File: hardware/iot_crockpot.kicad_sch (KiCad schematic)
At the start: 18 parts, among them J1 Screw_Terminal_01x02, K1 G5LE-1, K2 G5LE-1, Q1 2N7002, Q2 2N7002, U3 MAX31855KASA

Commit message: Schematic Updates - Power Supply
Added architecture for power supply to schematic.
Need to rethink control architecture. There is only two I/O exposed on
CYD. May use second MCU on control board flashed and controlled over
I2C by CYD.
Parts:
- added F2: Fuse, symbol Device:Fuse
- added F3: 1.5A, Fuse:Fuse_1206_3216Metric_Pad1.42x1.75mm_HandSolder, symbol Device:Polyfuse
- added J2: Screw_Terminal_01x02, symbol Connector:Screw_Terminal_01x02
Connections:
- net +5V: now also F3.2; no longer PS1.4 (+Vout)
- net NEUTRAL: now reaches C1.2, FL1.3, J1.1 (Pin_1), RV1.2
- net HOT: now reaches F1.1, J1.2 (Pin_2)
- new net: F3.1, PS1.4 (+Vout)
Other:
- note added: "120VAC INPUT"
- moved on the sheet: J1

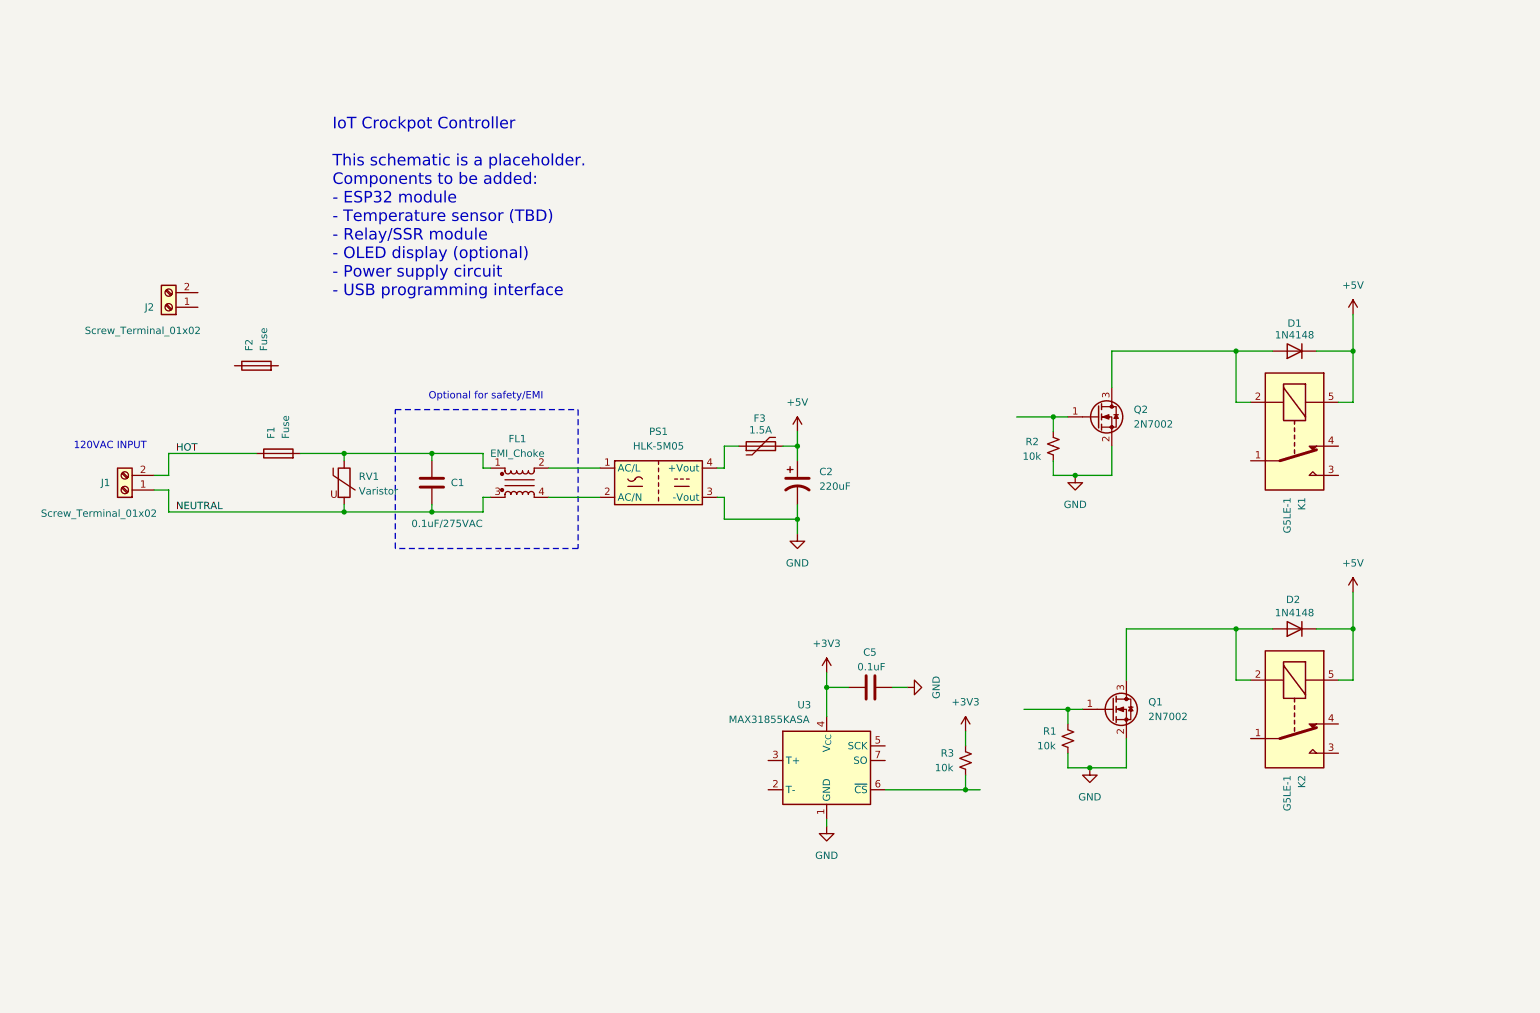
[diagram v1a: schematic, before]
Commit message: Added MCU to schematic
Added MCU to schematic and organized circuits into blocks
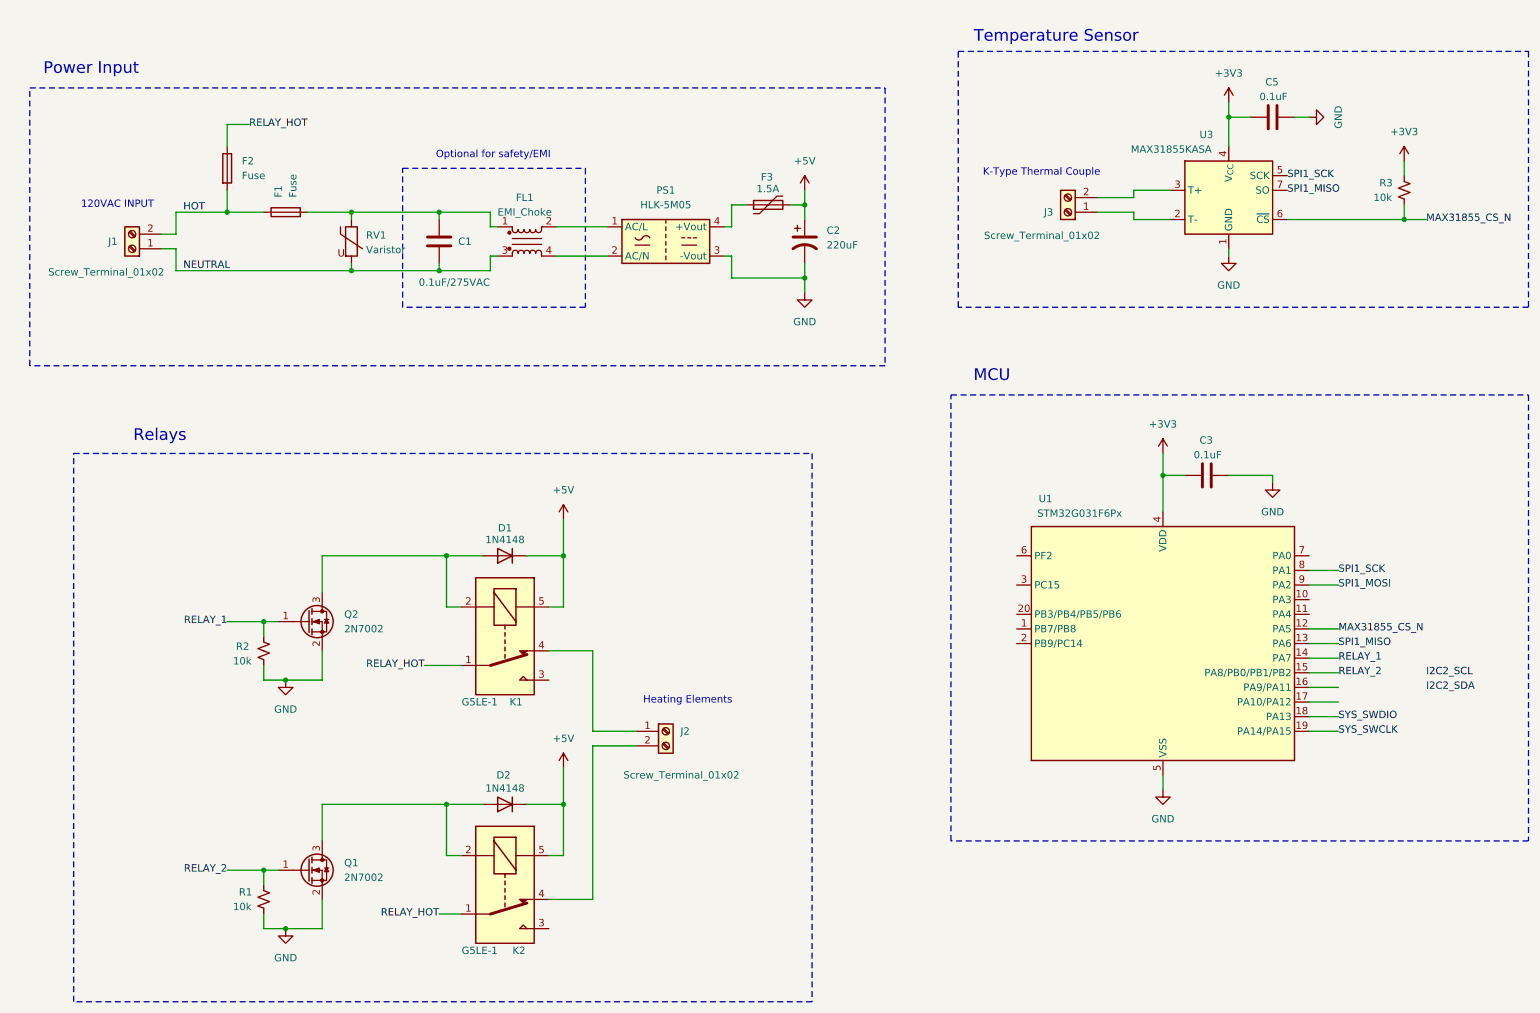
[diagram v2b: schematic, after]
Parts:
- added C3: 0.1uF, symbol Device:C
- added J3: Screw_Terminal_01x02, symbol Connector:Screw_Terminal_01x02
- added U1: STM32G031F6Px, Package_SO:TSSOP-20_4.4x6.5mm_P0.65mm, symbol MCU_ST_STM32G0:STM32G031F6Px
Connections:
- net +3V3: now also C3.1, U1.4 (VDD)
- net GND: now also C3.2, U1.5 (VSS)
- net HOT: now also F2.2
- net RELAY_1: now reaches Q2.1 (G), R2.1
- net RELAY_1: now also U1.14 (PA7)
- net RELAY_HOT: now reaches K2.1
- net RELAY_HOT: now also F2.1, K1.1
- net at K2.4: now also J2.2 (Pin_2)
- net at J2.1 (Pin_1): now also K1.4
- net at U3.2 (T-): now also J3.1 (Pin_1)
- net at U3.3 (T+): now also J3.2 (Pin_2)
- net SPI1_SCK: now reaches U3.5 (SCK)
- net SPI1_SCK: now also U1.8 (PA1)
- net MAX31855_CS_N: now reaches R3.2, U3.6 (~{CS})
- net MAX31855_CS_N: now also U1.12 (PA5)
- net SPI1_MISO: now reaches U3.7 (SO)
- net SPI1_MISO: now also U1.13 (PA6)
- net RELAY_2: now reaches Q1.1 (G), R1.1
- net RELAY_2: now also U1.15 (PA8/PB0/PB1/PB2)
- new net SPI1_MOSI: U1.9 (PA2)
- new net SYS_SWCLK: U1.19 (PA14/PA15)
- new net SYS_SWDIO: U1.18 (PA13)
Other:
- note added: "Heating Elements"
- note added: "K-Type Thermal Couple"
- note added: "MCU"
- note added: "Power Input"
- note added: "Relays"
- note added: "Temperature Sensor"
- note removed: "IoT Crockpot Controller This schematic is a placeholder. Components to be added: - ESP32 module - Temperature sensor (TBD) - Relay/SSR module - OLED display (optional) - Power supply circuit - USB programming interface"
- moved on the sheet: C1, C2, C5, D1, D2, F1, F2, F3, FL1, J1, J2, K1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

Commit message: More Passive Part Selection
Added passive parts/numbers and models to schematic.
Started rough outline of PCB. Considerations will need to be done for
angle of display in relation to height of components.
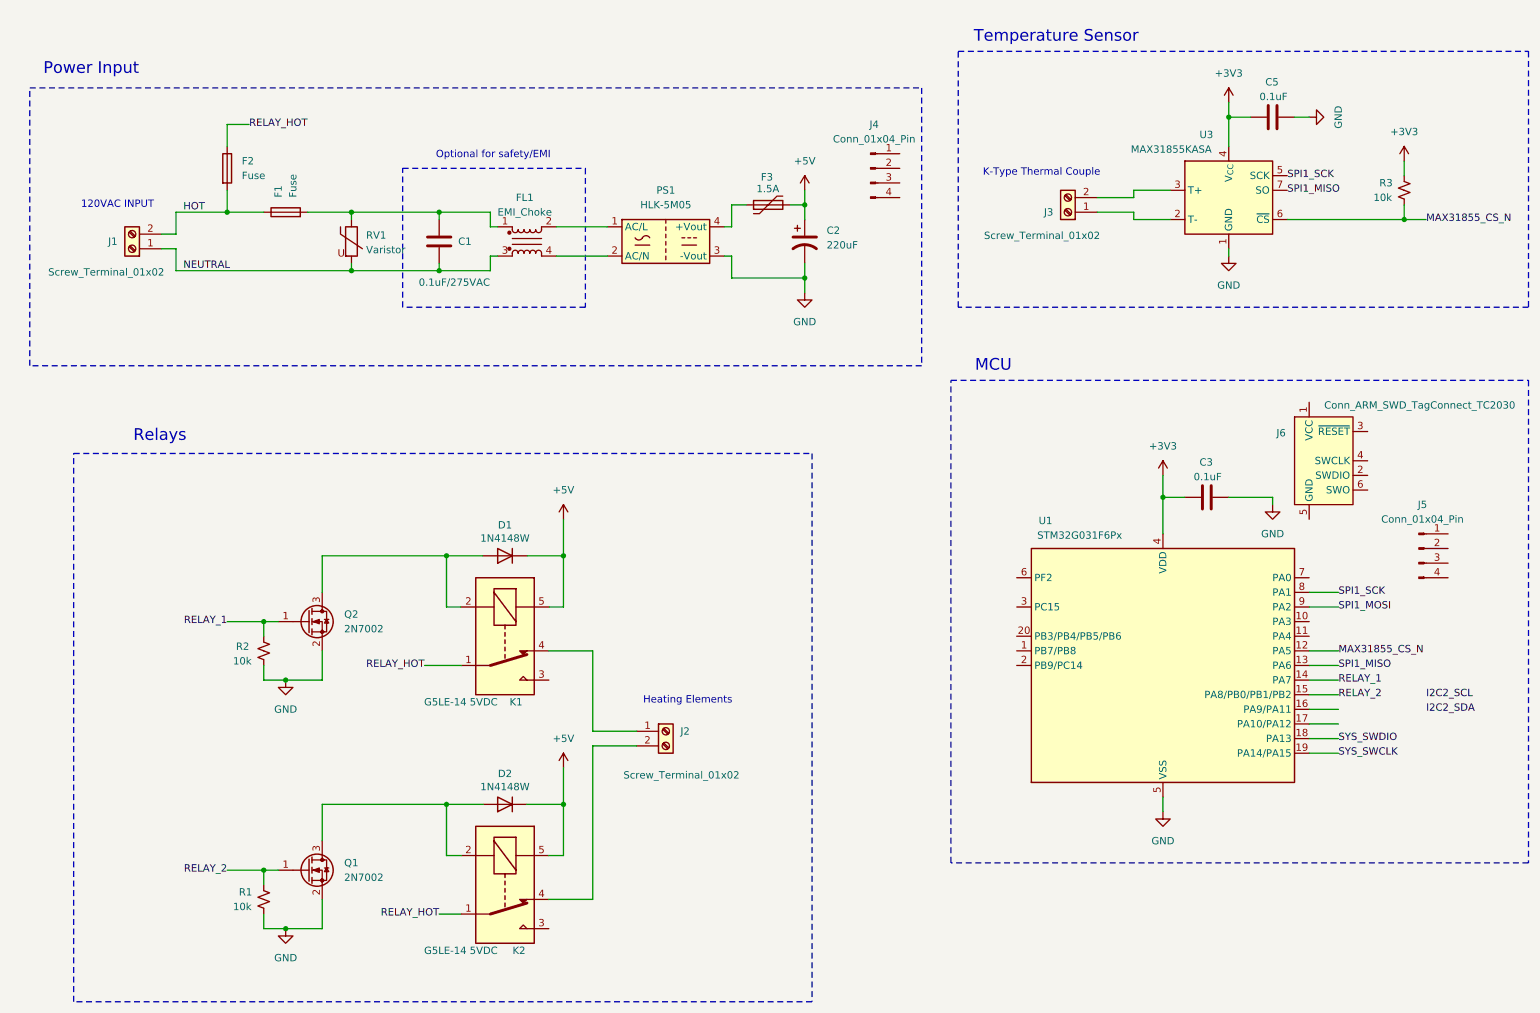
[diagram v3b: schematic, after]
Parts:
- removed D1, D2: 1N4148, Diode_THT:D_DO-35_SOD27_P7.62mm_Horizontal, symbol Diode:1N4148
- added D1, D2: 1N4148W, Diode_SMD:D_SOD-123, symbol Diode:1N4148W
- added J4, J5: Conn_01x04_Pin, Connector_JST:JST_GH_SM04B-GHS-TB_1x04-1MP_P1.25mm_Horizontal, symbol Connector:Conn_01x04_Pin
- added J6: Conn_ARM_SWD_TagConnect_TC2030, Connector:Tag-Connect_TC2030-IDC-FP_2x03_P1.27mm_Vertical, symbol Connector:Conn_ARM_SWD_TagConnect_TC2030
- C3, C5: footprint (none) -> Capacitor_SMD:C_0603_1608Metric_Pad1.08x0.95mm_HandSolder
- F1: footprint (none) -> Fuses:Fuseholder_Clip-5x20mm_Littelfuse_111_Inline_P20.00x5.00mm_D1.05mm_Horizontal_with_3D_body; Fuse Holder (none) -> 5x20mm - Xucheng Elec x 2; Manufacturer (none) -> Littelfuse; Part No (none) -> 0215.500MXP
- J1, J3: footprint (none) -> TerminalBlock_Phoenix:TerminalBlock_Phoenix_MKDS-1,5-2_1x02_P5.00mm_Horizontal; Manufacturer (none) -> Phoenix Contact; Part No (none) -> 1935161
- J2: footprint (none) -> TerminalBlock_Phoenix:TerminalBlock_Phoenix_MKDS-1,5-2_1x02_P5.00mm_Horizontal; Manufacturer (none) -> Phoenix Contact; Part No. (none) -> 1935161
- K1, K2: value G5LE-1 -> G5LE-14 5VDC
- R1, R2, R3: footprint (none) -> Resistor_SMD:R_0603_1608Metric
- RV1: footprint (none) -> Varistor:RV_Rect_V25S440P_L26.5mm_W8.2mm_P12.7mm; Manufacturer (none) -> BOURNS; Part No (none) -> MOV-10D561K
- U1: Manufacturer (none) -> ST Micro; Part No. (none) -> STM32G031F6Px
- U3: Manufacturer (none) -> Maxim Integrated; Part No. (none) -> MAX31855
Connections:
- net +5V: now also D1.1 (K), D2.1 (K)
- net at K2.2, Q1.3 (D): now also D2.2 (A)
- net at K1.2, Q2.3 (D): now also D1.2 (A)
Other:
- moved on the sheet: C3, U1

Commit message: Edited JST Connectors and created 3D model
Edited JST Connectors and created 3D model for use in
Fusion 360. This will drive where tall components will be placed on
PCB.
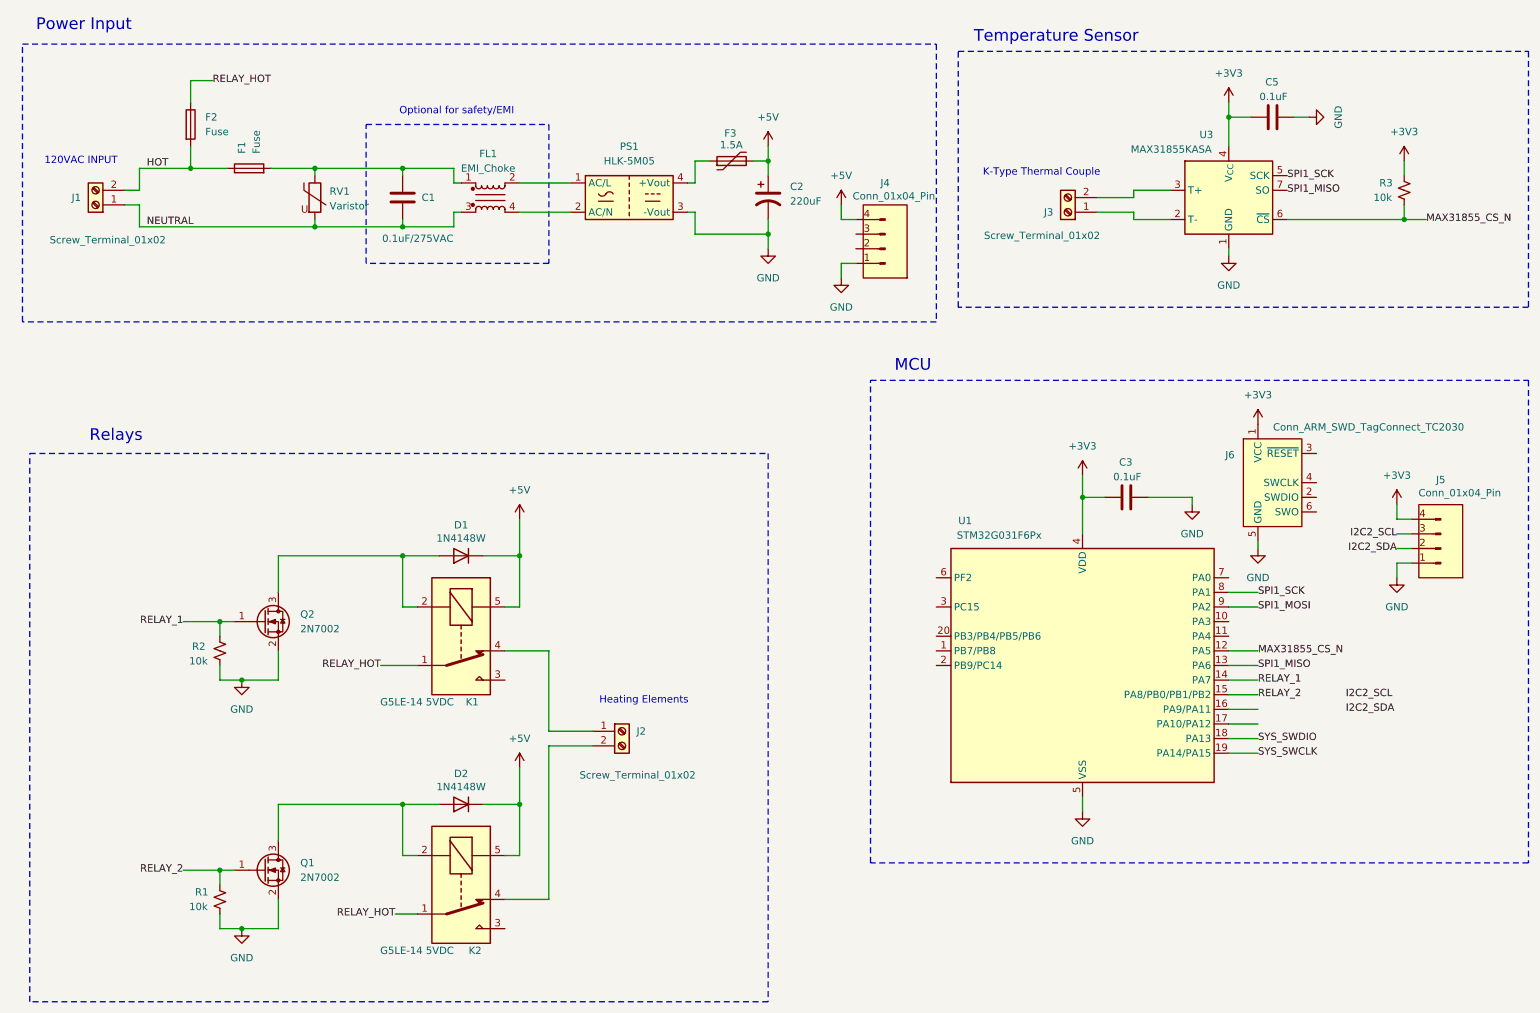
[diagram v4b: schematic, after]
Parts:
- removed J4, J5: Conn_01x04_Pin, Connector_JST:JST_GH_SM04B-GHS-TB_1x04-1MP_P1.25mm_Horizontal, symbol Connector:Conn_01x04_Pin
- added J4, J5: Conn_01x04_Pin, symbol Connectors:Conn_01x04_Pin
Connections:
- net +3V3: now also J6.1 (VCC), J5.4 (Pin_4)
- net +5V: now also J4.4 (Pin_4)
- net GND: now also J6.5 (GND), J4.1 (Pin_1), J5.1 (Pin_1)
- net I2C2_SCL: now also J5.3 (Pin_3)
- net I2C2_SDA: now also J5.2 (Pin_2)
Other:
- moved on the sheet: C1, C2, C3, D1, D2, F1, F2, F3, FL1, J1, J2, J6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
